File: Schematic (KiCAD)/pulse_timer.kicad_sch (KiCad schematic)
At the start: 50 parts, among them J66 Counter 4 Preload, J70 Counter 4 Preload

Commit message: - Pulse DAC logic is now complete.  - The 4-bit adders are verified correct using Excel.    - This revealed 1 tracing error and also 3 XNOR gates that are actually XOR in this case.  - Now including a PDF version of the schematic.
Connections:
- net at H86. (X): now also H83.2. (Y), H84. (X); no longer H85. (X)
- net at H83.2. (Y): now also H88. (X); no longer H83. (X)
- net at E37. (Y): now also E38. (X); no longer E34(b). (/Q2)
- net at E35. (X): now also G44. (X); no longer E34(b). (/Q2)
- net at E49. (X): now also E36. (X); no longer E34(b). (/Q2)
- net at H84. (X): now also H78. (X); no longer H82(a). (/Q2)
- net at G43. (X): now also G44. (X)
- net at H96. (X): now also H97. (X), H98. (X); no longer G100. (Ripple_Out)
- net at G92. (X): now also H98. (X); no longer G100. (Ripple_Out)
- net at E42. (X): now also E50. (X); no longer F7. (Ripple_Out)
- net at E50. (X): now also E39. (X), E43. (X); no longer E42. (X)
- new net: F6. (Ripple_Out), G23. (/Q2) (x3)
- new net: H85. (X), H86. (X)
- new net: H82(a). (/Q2), H83. (X), H94. (X)
- new net: H83. (X), H83.2. (Y)
- new net: E40. (/Q3), F4. (Ripple_Out) (x4)
- new net: E34(b). (/Q2), E37. (Y)
- new net: E34(b). (/Q2), E43. (X), G21. (X)
- new net: E34(b). (/Q2), E35. (X)
- new net: E34(b). (/Q2), E49. (X)
- new net: E34(b). (/Q2), E38. (X), E43. (X)
- new net: E35. (X), E37. (Y), E49. (X)
- new net: E37. (Y), F5. (X)
- new net: H109. (Ripple_Out), H93. (X), J66. (Ripple_Out)
- new net: H93. (X), J66. (Ripple_Out), J70. (Ripple_Out)
- new net: H82(b). (/Q), H93. (X)
- new net: E67. (/Q2), H109. (Ripple_Out) (x3)
- new net: F7. (Ripple_Out), G21. (X)
- new net: H82(a). (/Q2), H86. (X)
- new net: G91. (X), H82(a). (/Q2), H94. (X)
- new net: G100. (Ripple_Out), G91. (X)
- new net: E41. (/Q3), F3. (Ripple_Out) (x4)
- new net: E44. (X), F3. (Ripple_Out), F6. (Ripple_Out)
- new net: H82(a). (/Q2), H83.2. (Y)
- new net: H82(a). (/Q2), H84. (X)
- new net: H94. (X), H95. (X), H98. (X)
- new net: G100. (Ripple_Out), H96. (X)
- new net: G100. (Ripple_Out), G92. (X)
- new net: G84. (/Q3), J66. (Ripple_Out) (x4)
- new net: E39. (X), E42. (X), E52. (X)
- new net: E42. (X), F7. (Ripple_Out)
- new net: E44. (X), F3. (Ripple_Out), F4. (Ripple_Out)
- new net: G83. (/Q3), J70. (Ripple_Out) (x4)
- new net: H77. (X), H78. (X)
- new net: E34(a). (/Q), E44. (X)

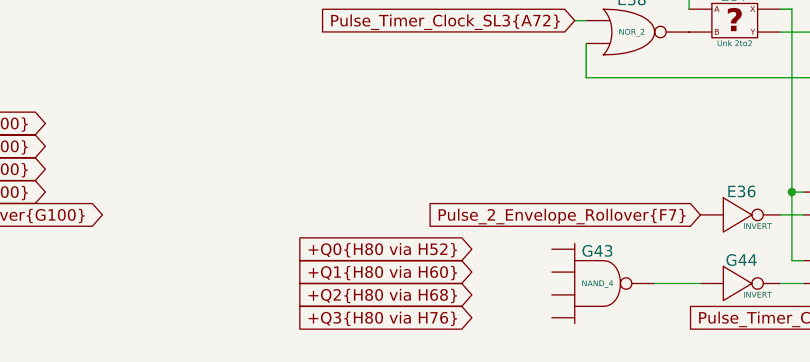
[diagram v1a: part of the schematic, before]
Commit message: Schematic Updates:  - Added all 10-bit CHR banking registers $5120 - $512B, including where all 10 bits come from when written.  - Added 8-bit CHR bank register $5202, which is the bank used when rendering the V-Split region.    + V-Split seems to always be 8-bit, 8kB bank regardless of CHR mode.  The wiki doesn't say that and I don't know for sure.  - Added decoding logic that activates the correct CHR bank for CHR A10, A11, A12 (corresponding to columns AV, AW, AX).  - Noted, AX15 activates $5202 CHR Bank for V-Split region.  AX16 activates CHR Bank from data stored in ExRAM for extended attributes.  Therefore, AX15 driven by AT1 High means we specifically are in v-split region, and not extended attribute mode.  With this knowledge, backtracking up the chain from AT1 to N14 sheds very useful insight what the 3-bit shift register at N11/N12/N13 is doing.  We now know that N14 goes low specifically for pattern table fetches when rendering the V-split region, and does not appear dual-purposed for extended attribute fetch sequencing.  This may seem rather subtle or unimportant, but it is a good advancement for higher level understanding what that mysterious shift register might be doing.
SVG Trace Updates:
 - Registers $5120, 5121, 5122, 5123 (first 4 CHR bank register), the outputs were labeled in reverse order.
 - Register $5130 (highest CHR bank bits), the outputs were labeled with backwards polarity.  The error was not having taken into account that the CPU data bus input to the latches came already inverted to begin with.
 - Still wrong: Cell AV7, 2-input NAND gate.  One of the inputs is missing and it logically should be driven by AS19 like the 4 cells to its direct right.  I can't quite make out how it makes that connection.
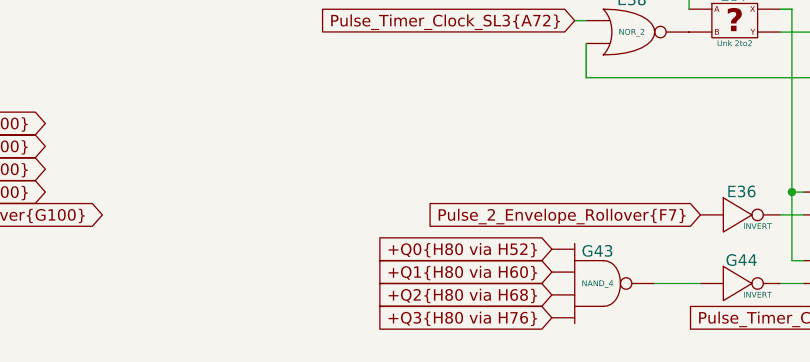
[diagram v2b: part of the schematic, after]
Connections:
- net +Q0{H80 via H52}: now also G43. (X)
- net +Q1{H80 via H60}: now also G43. (X)
- net +Q2{H80 via H68}: now also G43. (X)
- net +Q3{H80 via H76}: now also G43. (X)
- net at H86. (X): now also H83.2. (Y), H84. (X); no longer H85. (X)
- net at H83.2. (Y): now also H88. (X); no longer H83. (X)
- net at E37. (Y): now also E38. (X); no longer E34(b). (/Q2)
- net at E35. (X): now also G44. (X); no longer E34(b). (/Q2)
- net at E49. (X): now also E36. (X); no longer E34(b). (/Q2)
- net at H84. (X): now also H78. (X); no longer H82(a). (/Q2)
- net at H96. (X): now also H97. (X), H98. (X); no longer G100. (Ripple_Out)
- net at G92. (X): now also H98. (X); no longer G100. (Ripple_Out)
- net at E42. (X): now also E50. (X); no longer F7. (Ripple_Out)
- net at E50. (X): now also E39. (X), E43. (X); no longer E42. (X)
- new net: F6. (Ripple_Out), G23. (/Q2) (x3)
- new net: H85. (X), H86. (X)
- new net: H82(a). (/Q2), H83. (X), H94. (X)
- new net: H83. (X), H83.2. (Y)
- new net: E40. (/Q3), F4. (Ripple_Out) (x4)
- new net: E34(b). (/Q2), E37. (Y)
- new net: E34(b). (/Q2), E43. (X), G21. (X)
- new net: E34(b). (/Q2), E35. (X)
- new net: E34(b). (/Q2), E49. (X)
- new net: E34(b). (/Q2), E38. (X), E43. (X)
- new net: E35. (X), E37. (Y), E49. (X)
- new net: E37. (Y), F5. (X)
- new net: H109. (Ripple_Out), H93. (X), J66. (Ripple_Out)
- new net: H93. (X), J66. (Ripple_Out), J70. (Ripple_Out)
- new net: H82(b). (/Q), H93. (X)
- new net: E67. (/Q2), H109. (Ripple_Out) (x3)
- new net: F7. (Ripple_Out), G21. (X)
- new net: H82(a). (/Q2), H86. (X)
- new net: G91. (X), H82(a). (/Q2), H94. (X)
- new net: G100. (Ripple_Out), G91. (X)
- new net: E41. (/Q3), F3. (Ripple_Out) (x4)
- new net: E44. (X), F3. (Ripple_Out), F6. (Ripple_Out)
- new net: H82(a). (/Q2), H83.2. (Y)
- new net: H82(a). (/Q2), H84. (X)
- new net: G43. (X), G44. (X)
- new net: H94. (X), H95. (X), H98. (X)
- new net: G100. (Ripple_Out), H96. (X)
- new net: G100. (Ripple_Out), G92. (X)
- new net: G84. (/Q3), J66. (Ripple_Out) (x4)
- new net: E39. (X), E42. (X), E52. (X)
- new net: E42. (X), F7. (Ripple_Out)
- new net: E44. (X), F3. (Ripple_Out), F4. (Ripple_Out)
- new net: G83. (/Q3), J70. (Ripple_Out) (x4)
- new net: H77. (X), H78. (X)
- new net: E34(a). (/Q), E44. (X)
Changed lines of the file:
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@@
 	(global_label "+Q1{H80 via H60}"
 		(shape input)
-		(at 229.87 154.94 180)
-		(fields_autoplaced yes)
-		(effects
-			(font
-				(size 1.27 1.27)
-			)
-			(justify right)
-		)
-		(property "Intersheetrefs" "${INTERSHEET_REFS}"
-			(at 208.9234 154.94 0)
+		(at 238.76 154.94 180)
+		(fields_autoplaced yes)
+		(effects
+			(font
+				(size 1.27 1.27)
+			)
+			(justify right)
+		)
+		(property "Intersheetrefs" "${INTERSHEET_REFS}"
+			(at 217.8134 154.94 0)
 			(effects
 				(font
@@
 	(global_label "+Q2{H80 via H68}"
 		(shape input)
-		(at 229.87 157.48 180)
-		(fields_autoplaced yes)
-		(effects
-			(font
-				(size 1.27 1.27)
-			)
-			(justify right)
-		)
-		(property "Intersheetrefs" "${INTERSHEET_REFS}"
-			(at 208.9234 157.48 0)
+		(at 238.76 157.48 180)
+		(fields_autoplaced yes)
+		(effects
+			(font
+				(size 1.27 1.27)
+			)
+			(justify right)
+		)
+		(property "Intersheetrefs" "${INTERSHEET_REFS}"
+			(at 217.8134 157.48 0)
 			(effects
 				(font
@@
 	(global_label "+Q0{H80 via H52}"
 		(shape input)
-		(at 229.87 152.4 180)
-		(fields_autoplaced yes)
-		(effects
-			(font
-				(size 1.27 1.27)
-			)
-			(justify right)
-		)
-		(property "Intersheetrefs" "${INTERSHEET_REFS}"
-			(at 250.8166 152.4 0)
+		(at 238.76 152.4 180)
+		(fields_autoplaced yes)
+		(effects
+			(font
+				(size 1.27 1.27)
+			)
+			(justify right)
+		)
+		(property "Intersheetrefs" "${INTERSHEET_REFS}"
+			(at 259.7066 152.4 0)
 			(effects
 				(font
@@
 	(global_label "+Q3{H80 via H76}"
 		(shape input)
-		(at 229.87 160.02 180)
-		(fields_autoplaced yes)
-		(effects
-			(font
-				(size 1.27 1.27)
-			)
-			(justify right)
-		)
-		(property "Intersheetrefs" "${INTERSHEET_REFS}"
-			(at 208.9234 160.02 0)
-			(effects
-				(font
+		(at 238.76 160.02 180)
+		(fields_autoplaced yes)
+		(effects
+			(font
+				(size 1.27 1.27)
+			)
+			(justify right)
+		)
+		(property "Intersheetrefs" "${INTERSHEET_REFS}"
+			(at 217.8134 160.02 0)
+			(effects
+				(font

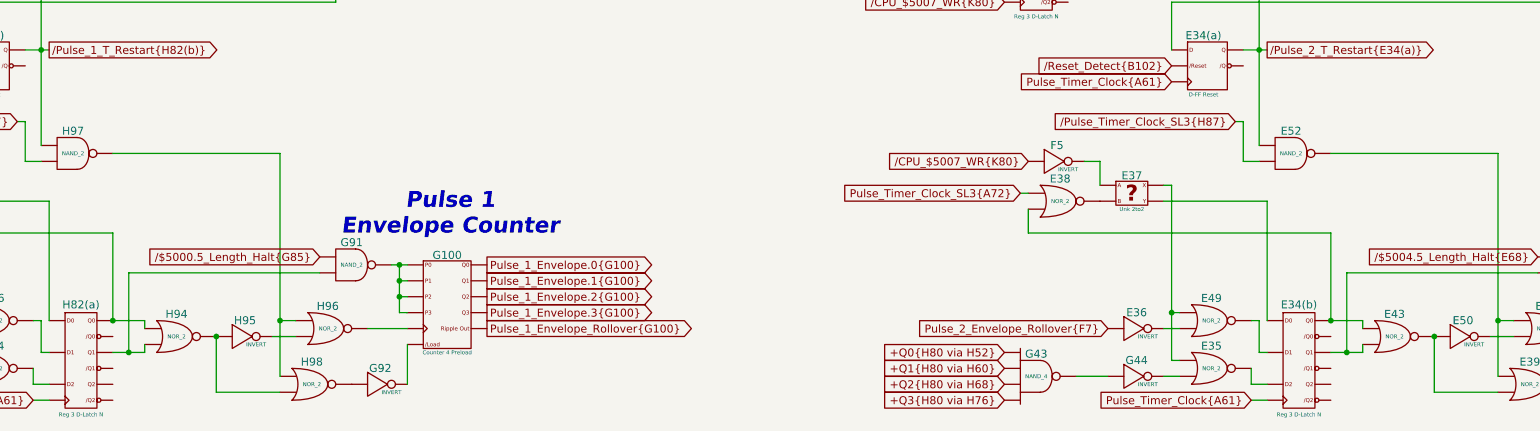
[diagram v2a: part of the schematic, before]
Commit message: - All cells in the left and center areas have now been added into the schematics.  - Changed naming of the PDF files; I was accidentally writing over furrtek's original with my new PDF.
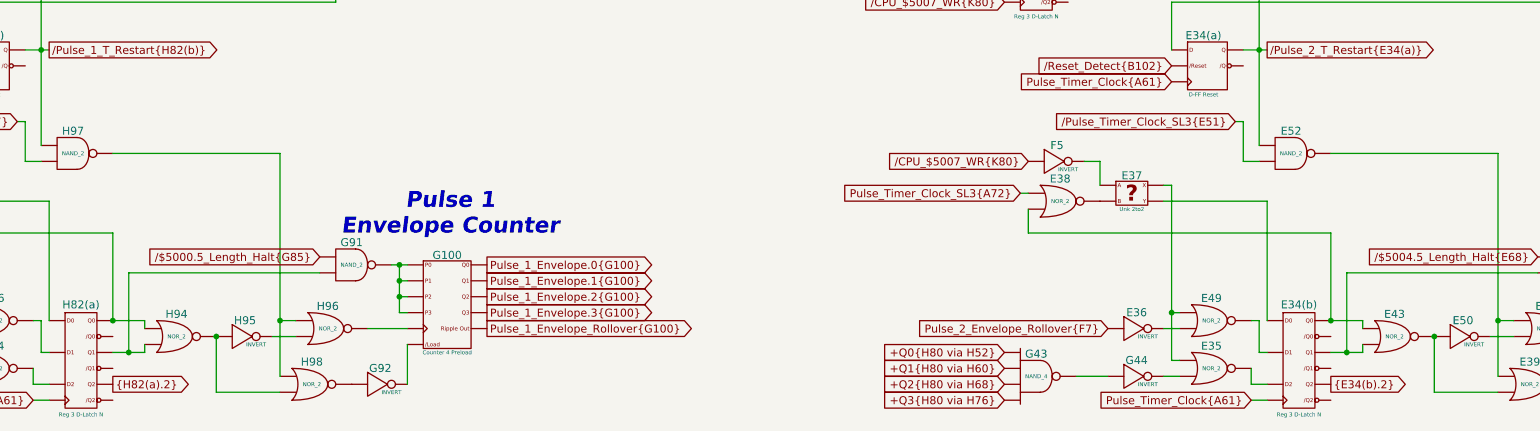
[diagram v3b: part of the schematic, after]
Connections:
- net /Pulse_Timer_Clock_SL3{H87}: no longer E52. (X)
- net at H86. (X): now also H83.2. (Y), H84. (X); no longer H85. (X)
- net at H83.2. (Y): now also H88. (X); no longer H83. (X)
- net {E34(b).2}: now reaches E34(b). (/Q2)
- net at E37. (Y): now also E38. (X); no longer E34(b). (/Q2)
- net at E35. (X): now also G44. (X); no longer E34(b). (/Q2)
- net at E49. (X): now also E36. (X); no longer E34(b). (/Q2)
- net {H82(a).2}: now reaches H82(a). (/Q2)
- net {H82(a).2}: no longer H86. (X)
- net at H84. (X): now also H78. (X); no longer H82(a). (/Q2)
- net at H96. (X): now also H97. (X), H98. (X); no longer G100. (Ripple_Out)
- net at G92. (X): now also H98. (X); no longer G100. (Ripple_Out)
- net at E42. (X): now also E50. (X); no longer F7. (Ripple_Out)
- net at E50. (X): now also E39. (X), E43. (X); no longer E42. (X)
- new net: F6. (Ripple_Out), G23. (/Q2) (x3)
- new net: H85. (X), H86. (X)
- new net: H82(a). (/Q2), H83. (X), H94. (X)
- new net: H83. (X), H83.2. (Y)
- new net: E40. (/Q3), F4. (Ripple_Out) (x4)
- new net: E34(b). (/Q2), E37. (Y)
- new net: E34(b). (/Q2), E43. (X), G21. (X)
- new net: E34(b). (/Q2), E35. (X)
- new net: E34(b). (/Q2), E49. (X)
- new net: E34(b). (/Q2), E38. (X), E43. (X)
- new net: E35. (X), E37. (Y), E49. (X)
- new net: E37. (Y), F5. (X)
- new net: H109. (Ripple_Out), H93. (X), J66. (Ripple_Out)
- new net: H93. (X), J66. (Ripple_Out), J70. (Ripple_Out)
- new net: H82(b). (/Q), H93. (X)
- new net: E67. (/Q2), H109. (Ripple_Out) (x3)
- new net: F7. (Ripple_Out), G21. (X)
- new net: H82(a). (/Q2), H86. (X)
- new net: G91. (X), H82(a). (/Q2), H94. (X)
- new net: G100. (Ripple_Out), G91. (X)
- new net: E41. (/Q3), F3. (Ripple_Out) (x4)
- new net: E44. (X), F3. (Ripple_Out), F6. (Ripple_Out)
- new net: H82(a). (/Q2), H83.2. (Y)
- new net: H82(a). (/Q2), H84. (X)
- new net: G43. (X), G44. (X)
- new net: H94. (X), H95. (X), H98. (X)
- new net: G100. (Ripple_Out), H96. (X)
- new net: G100. (Ripple_Out), G92. (X)
- new net: G84. (/Q3), J66. (Ripple_Out) (x4)
- new net: E39. (X), E42. (X), E52. (X)
- new net: E42. (X), F7. (Ripple_Out)
- new net: E44. (X), F3. (Ripple_Out), F4. (Ripple_Out)
- new net: G83. (/Q3), J70. (Ripple_Out) (x4)
- new net: H77. (X), H78. (X)
- new net: E34(a). (/Q), E44. (X)
- new net /Pulse_Timer_Clock_SL3{E51}: E52. (X)
